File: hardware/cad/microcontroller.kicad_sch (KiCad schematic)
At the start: 9 parts, among them J16 Conn_01x04_Pin, SW3 PTS645SH43SMTR92 LFS, SW4 SW_DPDT_x2, U3 ADG5434, U4 STM32L011F4Ux

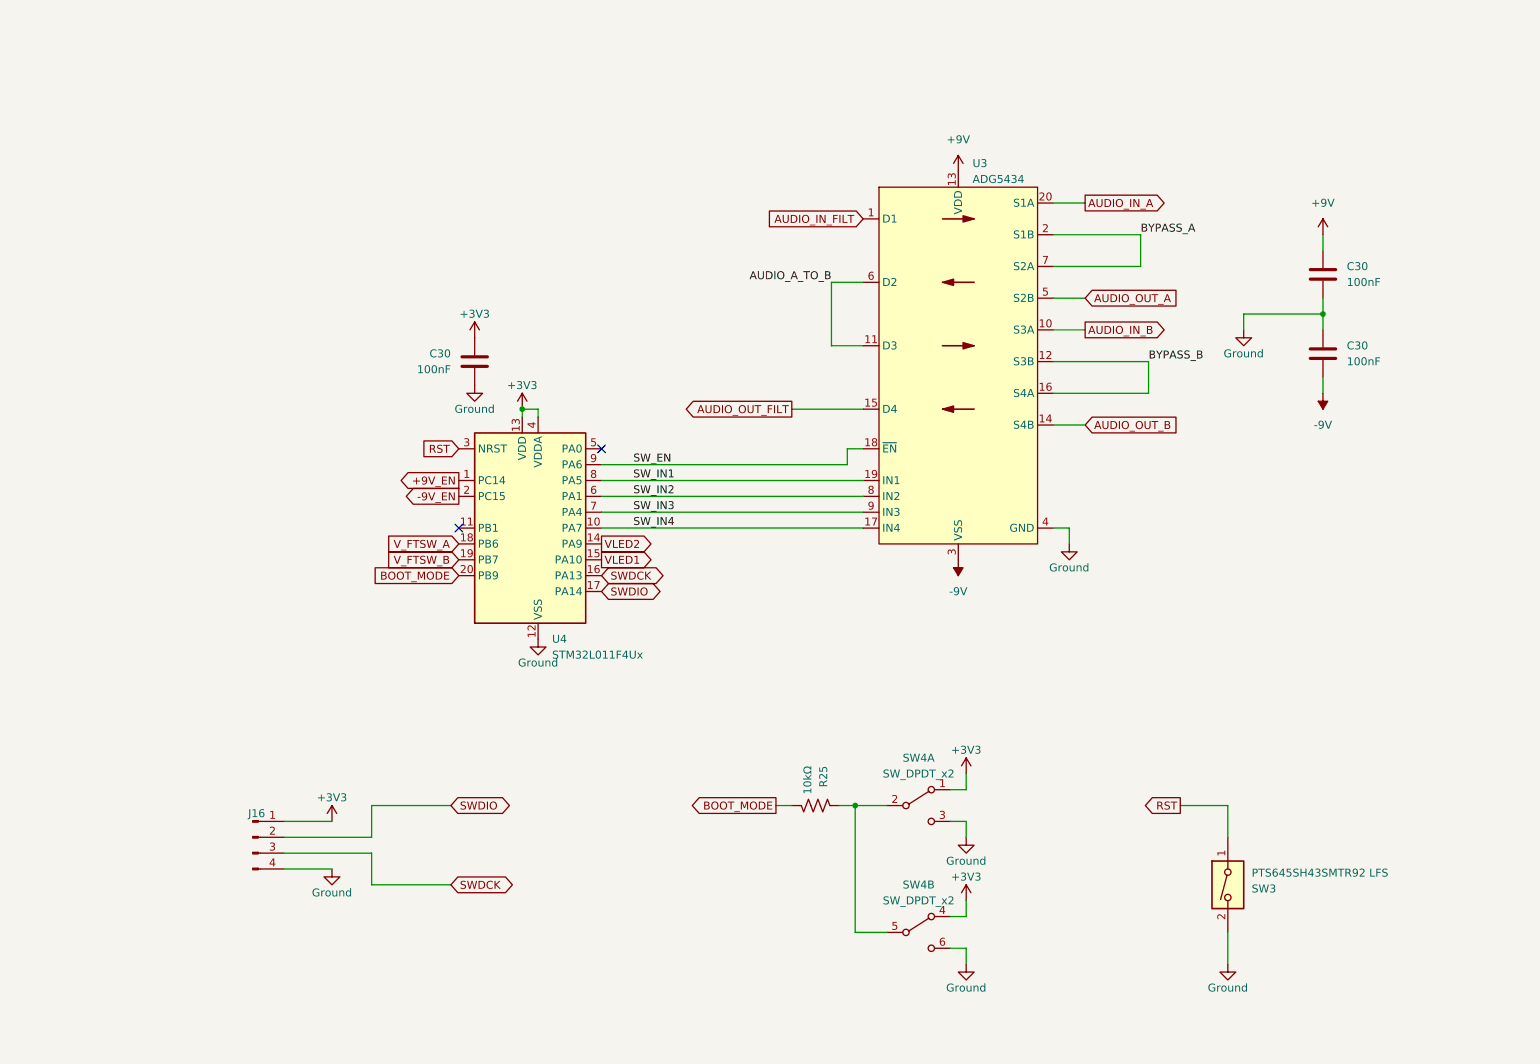
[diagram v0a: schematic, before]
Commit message: added differential inputs and started new layout
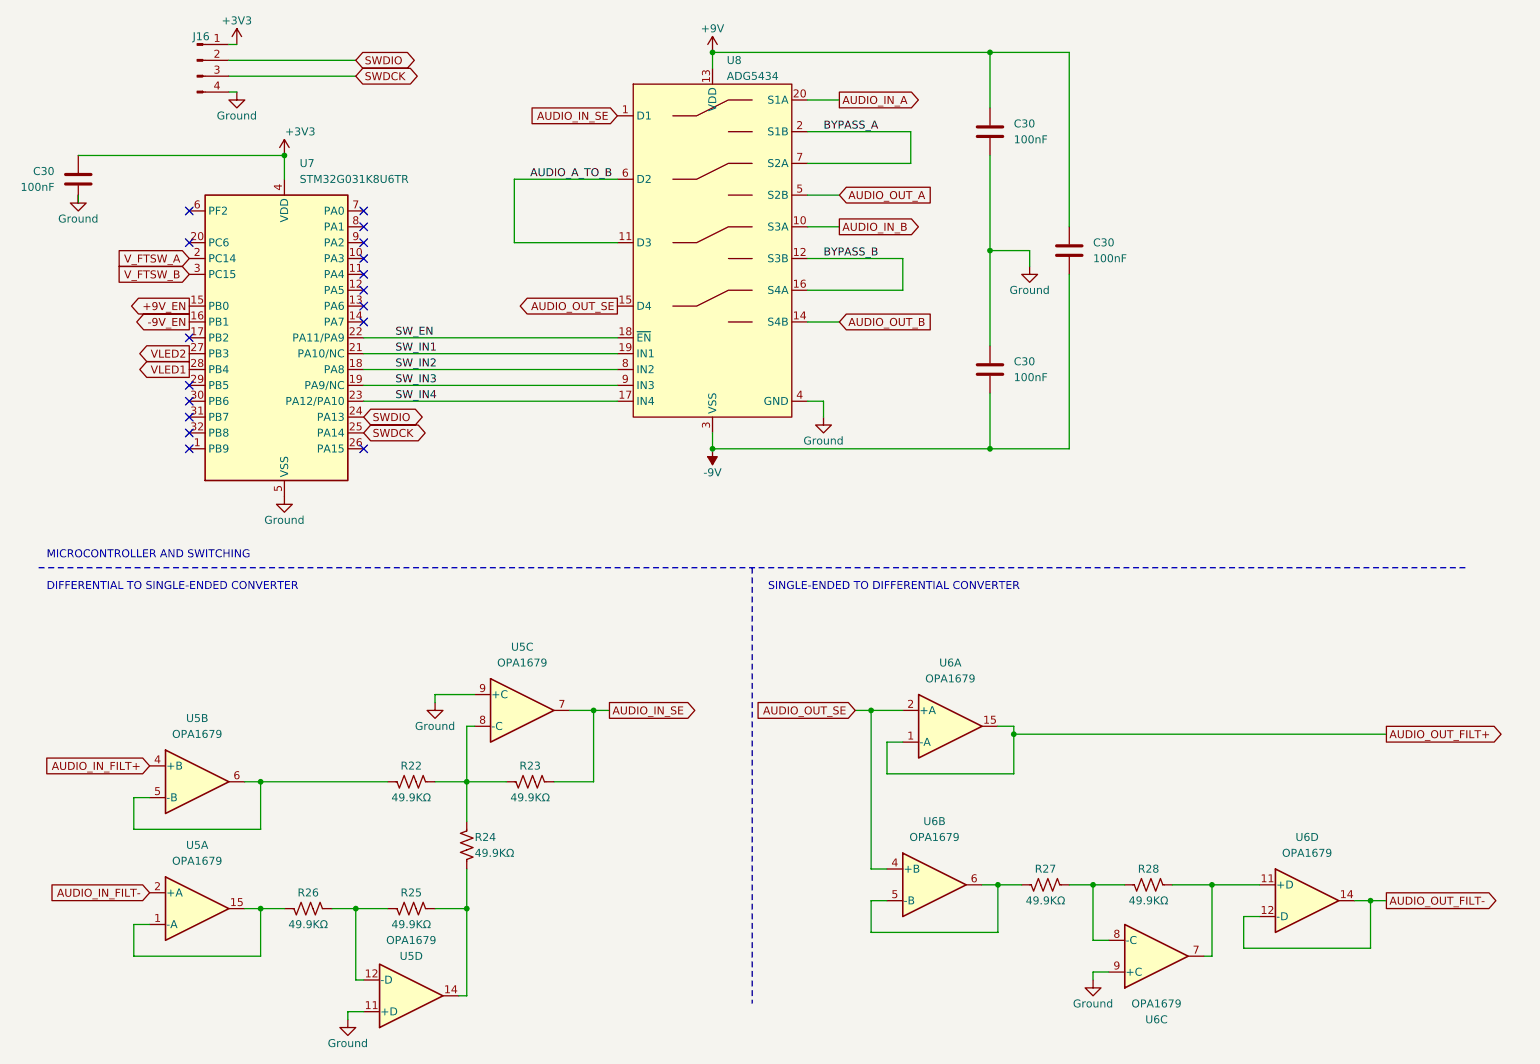
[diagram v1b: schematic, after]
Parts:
- removed SW3: PTS645SH43SMTR92 LFS, Button_Switch_SMD:SW_SPST_PTS645, symbol Switch:SW_DIP_x01
- removed SW4: SW_DPDT_x2, Button_Switch_SMD:SW_DPDT_CK_JS202011JCQN, symbol Switch:SW_DPDT_x2
- removed U4: STM32L011F4Ux, Library:ST_UFQFPN-20_3x3mm_P0.5mm, symbol MCU_ST_STM32L0:STM32L011F4Ux
- added C30: 100nF, Capacitor_SMD:C_0603_1608Metric, symbol Device:C
- added R22, R23, R24, R26, R27, R28: 49.9KΩ, Resistor_SMD:R_0603_1608Metric, symbol Device:R_US
- added U5, U6: OPA1679, Library:OPA1679, symbol Library:OPA1679
- added U7: STM32G031K8U6TR, Package_DFN_QFN:QFN-32-1EP_5x5mm_P0.5mm_EP3.45x3.45mm_ThermalVias, symbol MCU_ST_STM32G0:STM32G031K8Ux
- C30: footprint Capacitor_SMD:C_0805_2012Metric -> Capacitor_SMD:C_0603_1608Metric; Part Number GRM31C5C1H104JA01K -> GCJ188R71H104KA12D
- J16: footprint Connector_PinHeader_2.54mm:PinHeader_2x02_P2.54mm_Vertical_SMD -> Connector_PinHeader_1.27mm:PinHeader_1x04_P1.27mm_Vertical_SMD_Pin1Left
- R25: value 10kΩ -> 49.9KΩ; Part Number RN73H1JTTD1002F100 -> RN73H1JTTD1004F100
- U8: renamed from U3; footprint Library:LFCSP-20-1EP_4x4mm_P0.5mm_EP2.6x2.6mm -> Package_CSP:LFCSP-20-1EP_4x4mm_P0.5mm_EP2.6x2.6mm
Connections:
- net +3V3: now also U7.4 (VDD)
- net +9V: now also C30.2
- net +9V_EN: now also U7.15 (PB0)
- net -9V: now also C30.1
- net -9V_EN: now also U7.16 (PB1)
- net GND: now also U5.11 (+D), U5.9 (+C), U6.9 (+C), U7.33 (VSS), U7.5 (VSS)
- net SWDCK: now also U7.25 (PA14)
- net SWDIO: now also U7.24 (PA13)
- net SW_EN: now also U7.22 (PA11/PA9)
- net SW_IN1: now also U7.21 (PA10/NC)
- net SW_IN2: now also U7.18 (PA8)
- net SW_IN3: now also U7.19 (PA9/NC)
- net SW_IN4: now also U7.23 (PA12/PA10)
- net VLED1: now also U7.28 (PB4)
- net VLED2: now also U7.27 (PB3)
- net V_FTSW_A: now also U7.2 (PC14)
- net V_FTSW_B: now also U7.3 (PC15)
- net at R25.1: now also R26.2, U5.12 (-D)
- net AUDIO_IN_FILT renamed AUDIO_IN_SE
- net AUDIO_IN_SE: now also R23.2, U5.7
- net AUDIO_OUT_FILT renamed AUDIO_OUT_SE
- net AUDIO_OUT_SE: now also U6.2 (+A), U6.4 (+B)
- net BOOT_MODE: no longer names the net of R25.2
- net BOOT_MODE: now also R24.1, U5.14
- new net: R22.2, R23.1, R24.2, U5.8 (-C)
- new net: R22.1, U5.5 (-B), U5.6
- new net: R27.1, U6.5 (-B), U6.6
- new net: R27.2, R28.1, U6.8 (-C)
- new net: R28.2, U6.11 (+D), U6.7
- new net: R26.1, U5.1 (-A), U5.15
- new net AUDIO_IN_FILT+: U5.4 (+B)
- new net AUDIO_IN_FILT-: U5.2 (+A)
- new net AUDIO_OUT_FILT+: U6.1 (-A), U6.15
- new net AUDIO_OUT_FILT-: U6.12 (-D), U6.14
- no-connect marks 2 -> 17
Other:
- note added: "DIFFERENTIAL TO SINGLE-ENDED CONVERTER"
- note added: "MICROCONTROLLER AND SWITCHING"
- note added: "SINGLE-ENDED TO DIFFERENTIAL CONVERTER"
- moved on the sheet: C30, J16

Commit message: more layout updates
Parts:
- removed C30: 100nF, Capacitor_SMD:C_0603_1608Metric, symbol Device:C
- C30: value 100nF -> 100n
- R22, R23, R24, R25, R26, R27, R28: value 49.9KΩ -> 49.9K
- U8: footprint Package_CSP:LFCSP-20-1EP_4x4mm_P0.5mm_EP2.6x2.6mm -> Package_CSP:LFCSP-20-1EP_4x4mm_P0.5mm_EP2.6x2.6mm_ThermalVias
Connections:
- net AUDIO_OUT_FILT+: now also U6.12 (-D), U6.14; no longer U6.1 (-A), U6.15
- net AUDIO_OUT_FILT-: now also U6.1 (-A), U6.15; no longer U6.12 (-D), U6.14
- net AUDIO_OUT_SE: now also U6.11 (+D), U6.9 (+C); no longer U6.2 (+A), U6.4 (+B)
- net GND: now also U6.4 (+B); no longer U6.9 (+C)
- net at R27.2, R28.1: now also U6.5 (-B); no longer U6.8 (-C)
- new net: R27.1, U6.7, U6.8 (-C)
- new net: R28.2, U6.2 (+A), U6.6
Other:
- moved on the sheet: C30, J16, U7, U8

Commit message: reorganized project
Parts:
- removed C30 (x2): 100n, Capacitor_SMD:C_0603_1608Metric, symbol Device:C
- removed R22, R23, R24, R25, R26, R27, R28: 49.9K, Resistor_SMD:R_0603_1608Metric, symbol Device:R_US
- removed U5, U6: OPA1679, Library:OPA1679, symbol Library:OPA1679
- removed U8: ADG5434, Package_CSP:LFCSP-20-1EP_4x4mm_P0.5mm_EP2.6x2.6mm_ThermalVias, symbol Library:Analog_Devices_ADG5433
- added C38 (x4): 100n, Capacitor_SMD:C_0402_1005Metric, symbol Device:C
- added C418 (x2): 2.2µ, Capacitor_SMD:C_0603_1608Metric, symbol Device:C
- added D201 (x2): RSB10JS2, Library:RSB12JS2, symbol Library:ROHM_RSB12JS2
- added D303, D304: RED LED, N/A, symbol Library:LED
- added FID301, FID302, FID303: Fiducial, Fiducial:Fiducial_0.5mm_Mask1mm, symbol Mechanical:Fiducial
- added G301: OSHW LOGO, Symbol:OSHW-Logo_7.5x8mm_SilkScreen, symbol Graphic:Logo_Open_Hardware_Small
- added G302: ESD SYMBOL, Symbol:ESD-Logo_8.9x8mm_SilkScreen, symbol Graphic:SYM_ESD_Large
- added J301, J304, J306, J308: 6-440054-2, Library:TE_HPI_2.0MM_PITCH_MALE_HEADER_2POS, symbol Connector:Conn_01x02_Pin
- added J302, J305, J307, J309: 6-440129-2, N/A, symbol Connector:Conn_01x02_Socket
- added N1: 1590N1, N/A, symbol Mechanical:Housing
- added Q301, Q302: DMN2050, Library:DMN2050LFDB, symbol Device:Q_Dual_NMOS_S1G1D2S2G2D1
- added R208 (x2): 49.9k, Resistor_SMD:R_0402_1005Metric, symbol Device:R_US
- added R404 (x4): 750R, Resistor_SMD:R_0402_1005Metric, symbol Device:R_US
- added R405 (x6): 120R, Resistor_SMD:R_0402_1005Metric, symbol Device:R_US
- added R410 (x2): 200R, Resistor_SMD:R_0603_1608Metric, symbol Device:R_US
- added R507 (x4): 15R, Resistor_SMD:R_0603_1608Metric, symbol Device:R_US
- added SW301, SW302: FOOTSWITCH, N/A, symbol Switch:SW_SPST
- added W301, W302: RED/WHT, N/A, symbol Library:Twisted_Pair
- added W303: RED/BLK, N/A, symbol Library:Twisted_Pair
- C18: renamed from C30; footprint Capacitor_SMD:C_0603_1608Metric -> Capacitor_SMD:C_0402_1005Metric; Part Number GCJ188R71H104KA12D -> GRM155R61H104KE19J
- J303: renamed from J16; value Conn_01x04_Pin -> 2x2 PIN HEADER; footprint Connector_PinHeader_1.27mm:PinHeader_1x04_P1.27mm_Vertical_SMD_Pin1Left -> Connector_PinHeader_2.54mm:PinHeader_2x02_P2.54mm_Vertical_SMD; Manufacturer (none) -> Sullins Connector Solutions; Part Number (none) -> GEC02DABN-M30
- U301: renamed from U7; value STM32G031K8U6TR -> STM32G031K8U6; footprint Package_DFN_QFN:QFN-32-1EP_5x5mm_P0.5mm_EP3.45x3.45mm_ThermalVias -> Library:QFN-32-1EP_5x5mm_P0.5mm_EP3.45x3.45mm; symbol MCU_ST_STM32G0:STM32G031K8Ux -> Library:STM32G031K8U6; Manufacturer (none) -> ST Microelectronics; Part Number (none) -> STM32G031K8U6TR
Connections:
- net +3V3: now also C38.2, C38.2, C38.2, C38.2, D201.1, D201.1, J301.2 (Pin_2), J304.2 (Pin_2), J306.2 (Pin_2), J308.2 (Pin_2), R410.1, R410.1
- net GND: now also C38.1, C38.1, C38.1, C38.1, C418.1, C418.1, D201.4, D201.4, Q301.1 (S), Q301.4 (S), Q302.1 (S), Q302.4 (S), R208.1, R208.1, R404.2, R404.2, R404.2, R404.2
- net SWDCK: now also D201.2, D201.5
- net SWDIO: now also D201.2, D201.5
- net VLED1 renamed LEDB_EN
- net LEDB_EN: now also R405.1
- net VLED2 renamed FTSW_B
- net FTSW_B: now also R405.2
- net V_FTSW_A renamed FTSW_A
- net FTSW_A: now also R405.2
- net V_FTSW_B renamed LEDA_EN
- net LEDA_EN: now also R405.1
- new net: Q301.6 (D), R405.1, R410.2
- new net: Q301.5 (G), R404.1, R405.2
- new net: Q302.5 (G), R404.1, R405.2
- new net: Q302.6 (D), R405.1, R410.2
- new net: J307.1 (Pin_1), SW302.1 (A)
- new net: J307.2 (Pin_2), SW302.2 (B)
- new net: D304.1 (K), J309.2 (Pin_2)
- new net: D304.2 (A), J309.1 (Pin_1)
- new net: Q302.2 (G), R404.1, R405.2
- new net: J302.1 (Pin_1), SW301.1 (A)
- new net: J302.2 (Pin_2), SW301.2 (B)
- new net: D303.2 (A), J305.1 (Pin_1)
- new net: D303.1 (K), J305.2 (Pin_2)
- new net: Q301.2 (G), R404.1, R405.2
- new net VS_A: Q302.3 (D), R507.2
- new net VS_B: Q301.3 (D), R507.2
- new net V_FTSW_FILT_A: C418.2, R208.2, R405.1, R507.2
- new net V_FTSW_FILT_B: C418.2, R208.2, R405.1, R507.2
- new net V_FTSW_RAW_A: J306.1 (Pin_1), R507.1
- new net V_FTSW_RAW_B: J301.1 (Pin_1), R507.1
- new net V_LEDA: J308.1 (Pin_1), R507.1
- new net V_LEDB: J304.1 (Pin_1), R507.1
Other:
- note added: "20AWG TWISTED PAIR"
- note added: "24AWG TWISTED PAIR"
- note added: "EFFECT A PERIPHERALS"
- note added: "EFFECT B PERIPHERALS"
- note added: "HAMMOND 1590N1 ENCLOSURE CAST ALUMINUM, UNPAINTED"
- note added: "I_LED = 45mA"
- note added: "I_PK = 220mA"
- note added: "I_PK = 27.5mA"
- note added: "PLACE BYPASS CAPACITORS AS CLOSE TO CONNECTORS OR ICS AS POSSIBLE PLACE SERIAL WIRE DEBUG HEADER NEAR MICROCONTROLLER PLACE FOOTSWITCH AND LED CIRCUITS CLOSE TO CONNECTORS"
- note added: "SERIAL WIRE DEBUG"
- note added: "SILKSCREEN LAYER"
- note removed: "DIFFERENTIAL TO SINGLE-ENDED CONVERTER"
- note removed: "SINGLE-ENDED TO DIFFERENTIAL CONVERTER"
- moved on the sheet: C18, J303

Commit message: finalized schematic
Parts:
- removed FID301, FID302, FID303: Fiducial, Fiducial:Fiducial_0.5mm_Mask1mm, symbol Mechanical:Fiducial
- removed G301: OSHW LOGO, Symbol:OSHW-Logo_7.5x8mm_SilkScreen, symbol Graphic:Logo_Open_Hardware_Small
- removed G302: ESD SYMBOL, Symbol:ESD-Logo_8.9x8mm_SilkScreen, symbol Graphic:SYM_ESD_Large
- removed N1: 1590N1, N/A, symbol Mechanical:Housing
- removed R507 (x2): 15R, Resistor_SMD:R_0603_1608Metric, symbol Device:R_US
- removed W301, W302: RED/WHT, N/A, symbol Library:Twisted_Pair
- removed W303: RED/BLK, N/A, symbol Library:Twisted_Pair
- added FID401: FIDUCIAL, Fiducial:Fiducial_0.5mm_Mask1mm, symbol Mechanical:Fiducial
- added R404 (x2): 120Ω, Resistor_SMD:R_0402_1005Metric, symbol Device:R_US
- added W401, W403: RED/WHT, N/A, symbol Library:Twisted_Pair
- added W402, W404: BLU/WHT, N/A, symbol Library:Twisted_Pair
- C18, C38: value 100n -> 100nF
- C418: value 2.2µ -> 2.2µF
- R208: value 49.9k -> 49.9kΩ
- R404: value 750R -> 750Ω
- R405: value 120R -> 120Ω
- R410: value 200R -> 200Ω
- R507: value 15R -> 15Ω
- renumbered D303 to D403, D304 to D404, J301 to J401, J302 to J402, J303 to J403, J304 to J404, J305 to J405, J306 to J406, J307 to J407, J308 to J408, J309 to J409, Q301 to Q401, Q302 to Q402, SW301 to SW401, SW302 to SW402, U301 to U401
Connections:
- net V_FTSW_FILT_A: now also R404.2
- net V_FTSW_FILT_B: now also R404.2
- net V_FTSW_RAW_A: now also R404.1
- net V_FTSW_RAW_B: now also R404.1
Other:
- note added: "24AWG TWISTED PAIR 10cm"
- note added: "24AWG TWISTED PAIR 5cm"
- note added: "EFFECT "A" PERIPHERALS"
- note added: "EFFECT "B" PERIPHERALS"
- note added: "I_PK = 25mA"
- note added: "PLACE BYPASS CAPACITORS AS CLOSE TO CONNECTORS OR ICS AS POSSIBLE PLACE SERIAL WIRE DEBUG HEADER NEAR MICROCONTROLLER PLACE FOOTSWITCH AND LED CIRCUITS CLOSE TO CONNECTORS PLACE DIGITAL AND LOW VOLTAGE COMPONENTS NEAR EACH OTHER AND AWAY FROM OTHER CIRCUITS"
- note removed: "20AWG TWISTED PAIR"
- note removed: "24AWG TWISTED PAIR"
- note removed: "EFFECT A PERIPHERALS"
- note removed: "EFFECT B PERIPHERALS"
- note removed: "HAMMOND 1590N1 ENCLOSURE CAST ALUMINUM, UNPAINTED"
- note removed: "I_PK = 220mA"
- note removed: "PLACE BYPASS CAPACITORS AS CLOSE TO CONNECTORS OR ICS AS POSSIBLE PLACE SERIAL WIRE DEBUG HEADER NEAR MICROCONTROLLER PLACE FOOTSWITCH AND LED CIRCUITS CLOSE TO CONNECTORS"
- note removed: "SILKSCREEN LAYER"
- company: Alessandro Rizzoni -> ALESSANDRO RIZZONI
- title: Baseboard -> BASEBOARD
